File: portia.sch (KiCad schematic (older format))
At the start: 64 parts, among them J1 USB_B_Micro, J10 Conn_01x02, J11 Conn_01x02, J12 Conn_01x02, J13 Conn_01x02, J14 Conn_01x02, J15 Conn_01x02, J16 Conn_01x04, J2 Conn_01x02, J3 Conn_01x02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

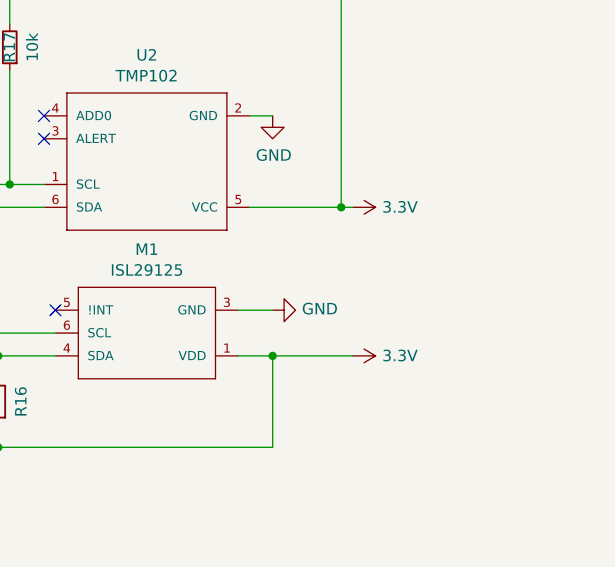
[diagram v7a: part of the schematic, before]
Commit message: fix i2c net list +3V3
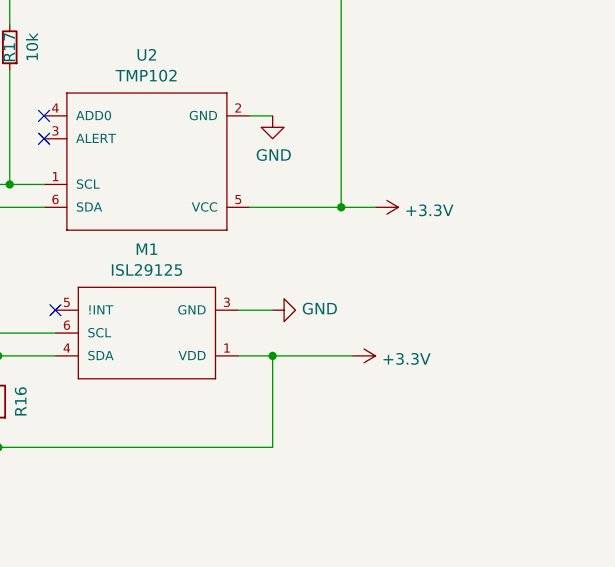
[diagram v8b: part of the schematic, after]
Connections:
- net 3.3V is gone; now on net +3V3: M1.1 (VDD), R12.1, R15.2, R16.1, R17.2, U2.5 (VCC)
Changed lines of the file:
@@
 	12300 8650 13500 8650
-$Comp
-L SparkFun-Aesthetics:3.3V #SUPPLY0101
-U 1 1 5C35ADBC
-P 15150 9300
-F 0 "#SUPPLY0101" H 15150 9300 50  0001 L BNN
-F 1 "3.3V" V 15150 9429 50  0000 L CNN
-F 2 "" H 15150 9300 50  0001 C CNN
-F 3 "" H 15150 9300 50  0001 C CNN
-	1    15150 9300
-	0    1    1    0
-$EndComp
 $Comp
 L Device:R_Small R17
@@
 Wire Wire Line
 	14700 8650 15100 8650
-$Comp
-L SparkFun-Aesthetics:3.3V #SUPPLY0102
-U 1 1 5C39E3C3
-P 15150 8650
-F 0 "#SUPPLY0102" H 15150 8650 50  0001 L BNN
-F 1 "3.3V" V 15150 8779 50  0000 L CNN
-F 2 "" H 15150 8650 50  0001 C CNN
-F 3 "" H 15150 8650 50  0001 C CNN
-	1    15150 8650
-	0    1    1    0
-$EndComp
 Wire Wire Line
 	14650 9100 14800 9100
@@
 	13650 7700 15100 7700
 Connection ~ 15100 8650
-Wire Wire Line
-	15100 8650 15150 8650
 NoConn ~ 13850 9100
 Wire Wire Line
@@
 $EndComp
 Wire Wire Line
-	7250 5350 7250 5450
-Connection ~ 7250 5450
-Wire Wire Line
 	7250 5450 7250 5600
 Connection ~ 7250 5600
@@
 	1    0    0    -1
 $EndComp
+$Comp
+L power:+3.3V #PWR0131
+U 1 1 5C37F7F1
+P 15250 8650
+F 0 "#PWR0131" H 15250 8500 50  0001 C CNN
+F 1 "+3.3V" V 15265 8778 50  0000 L CNN
+F 2 "" H 15250 8650 50  0001 C CNN
+F 3 "" H 15250 8650 50  0001 C CNN
+	1    15250 8650
+	0    1    1    0
+$EndComp
+Wire Wire Line
+	15100 8650 15250 8650
+$Comp
+L power:+3.3V #PWR0132
+U 1 1 5C3B54C5
+P 15150 9300
+F 0 "#PWR0132" H 15150 9150 50  0001 C CNN
+F 1 "+3.3V" V 15165 9428 50  0000 L CNN
+F 2 "" H 15150 9300 50  0001 C CNN
+F 3 "" H 15150 9300 50  0001 C CNN
+	1    15150 9300
+	0    1    1    0
+$EndComp
+Wire Wire Line
+	7250 5350 7250 5450
+Connection ~ 7250 5450
 $EndSCHEMATC
